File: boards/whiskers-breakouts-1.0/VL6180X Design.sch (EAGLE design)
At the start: 17 parts, among them Q1 BSS138, Q2 BSS138, U1 VL6180X, U3 MIC5225_2.8V, U4 VL6180X, U5 VL6180X

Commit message: Whiskers update
Updated the Whiskers board: routing and asthetics
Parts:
- removed C4, C6: 10uF, SparkFun-Capacitors:1.0NF/1000PF-0603-50V-10%
- removed C5: 0.1uF, SparkFun-Capacitors:1.0NF/1000PF-0603-50V-10%
- removed JP2: (no value), adafruit:PINHD-1X8BIG
- removed Q1, Q2: BSS138, microbuilder:MOSFET-NWIDE
- removed U$10: PINHD-1X10, adafruit:PINHD-1X10
- removed U3: MIC5225_2.8V, microbuilder:VREG_SOT23-5
- removed U4, U5: VL6180X, microbuilder:VL6180X
- added C3: 10uF, SparkFun-Capacitors:1.0NF/1000PF-0603-50V-10%
- added J1: FEMALE 2x3, SparkFun-Connectors:CONN_03X2FEMALE
- added Q3, Q4: BSS138, microbuilder:MOSFET-NWIDE
- added U2: MIC5225_2.8V, microbuilder:VREG_SOT23-5
- C1: value 0.1uF -> 10uF
- R1, R2, R3, R4: device adafruit:FLIPFLOP-RES -> SparkFun-Resistors:0.05OHM-0603-1/5W-1%
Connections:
- removed net INT_1: U1.GPIO1
- removed net INT_2: U5.GPIO1
- removed net INT_3: U4.GPIO1
- removed net N$10: U$10.9
- removed net N$5: U$10.6
- removed net N$6: JP2.6
- removed net N$7: JP2.7
- removed net N$8: U$10.7
- removed net N$9: U$10.8
- removed net OUT: C4.2, U3.OUT
- removed net RESET_1: U1.GPIO0
- removed net RESET_2: U5.GPIO0
- removed net RESET_3: U4.GPIO0
- new net VCC: C1.2, R1.2, R4.2, U2.OUT
- net +3.3V: now also C3.2, J1.1, Q3.G, Q4.G, U2.EN, U2.IN; no longer C1.1, C5.1, C6.2, JP2.1, Q1.G, Q2.G, R1.2, R4.2, U$10.1, U3.EN, U3.IN, U4.AVDD, U4.AVDD_VCS, U5.AVDD, U5.AVDD_VCS
- net GND: now also C1.1, C3.1, J1.6, U2.GND; no longer C1.2, C4.1, C5.2, C6.1, JP2.8, U$10.10, U3.GND, U4.AVSS, U4.AVSS_VCS, U5.AVSS, U5.AVSS_VCS
- net INT: now also J1.3, U1.GPIO1; no longer JP2.3, U$10.3
- net RST: now also J1.2, U1.GPIO0; no longer JP2.2, U$10.2
- net SCL_2.7V: now also Q3.S; no longer Q1.S, Q2.S, R1.1, U4.SCL, U5.SCL
- net SCL_3.3V: now also J1.4, Q3.D; no longer JP2.4, Q1.D, Q2.D, R2.1, U$10.4
- net SDA_2.7V: now also Q4.S, R2.1; no longer U4.SDA, U5.SDA
- net SDA_3.3V: now also J1.5, Q4.D, R1.1; no longer JP2.5, U$10.5
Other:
- note added: "Bi-directional LevelSshifter"
- note added: "Connector"
- note added: "Sensor"
- note added: "Voltage Regulator"

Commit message: adding one more sensor
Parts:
- added C4, C5: 0.1uF, SparkFun-Capacitors:1.0NF/1000PF-0603-50V-10%
- added R5, R6, R7: 47k, SparkFun-Resistors:0.05OHM-0603-1/5W-1%
- added U3, U4: VL6180X, microbuilder:VL6180X
- J1: value FEMALE 2x3 -> 7-PIN_2MM-V; device SparkFun-Connectors:CONN_03X2FEMALE -> RoboJackets-Connectors:7-PIN_2MM-V
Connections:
- removed net RST: J1.2, U1.GPIO0
- new net N$1: R5.2, U1.GPIO0
- new net N$2: R6.2, U3.GPIO0
- new net N$3: R7.2, U4.GPIO0
- new net RST_1: J1.2, R5.1
- new net RST_2: J1.3, R6.1
- new net RST_3: R7.1
- net +3.3V: now also C4.1, C5.1, U3.AVDD, U3.AVDD_VCS, U4.AVDD, U4.AVDD_VCS
- net GND: now also C4.2, C5.2, J1.7, U3.AVSS, U3.AVSS_VCS, U4.AVSS, U4.AVSS_VCS; no longer J1.6
- net INT: now also J1.4, U3.GPIO1, U4.GPIO1; no longer J1.3
- net SCL_2.7V: now also U3.SCL, U4.SCL
- net SCL_3.3V: now also J1.5; no longer J1.4
- net SDA_2.7V: now also U3.SDA, U4.SDA
- net SDA_3.3V: now also J1.6; no longer J1.5
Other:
- moved on the sheet: C2, U1

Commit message: latest
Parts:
- removed J1: 7-PIN_2MM-V, RoboJackets-Connectors:7-PIN_2MM-V
- added J2: 6-PIN_2MM-V, RoboJackets-Connectors:6-PIN_2MM-V
- C1, C3: value 10uF -> 1uF
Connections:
- net SCL_2.7V renamed SCL_2.8V
- net SDA_2.7V renamed SDA_2.8V
- removed net INT: J1.4, U1.GPIO1, U3.GPIO1, U4.GPIO1
- removed net N$1: R5.2, U1.GPIO0
- removed net N$2: R6.2, U3.GPIO0
- removed net N$3: R7.2, U4.GPIO0
- net +3.3V: now also J2.1; no longer C2.1, C4.1, C5.1, J1.1, U1.AVDD, U1.AVDD_VCS, U3.AVDD, U3.AVDD_VCS, U4.AVDD, U4.AVDD_VCS
- net GND: now also J2.6; no longer J1.7
- net RST_1: now also J2.2, U1.GPIO0; no longer J1.2
- net RST_2: now also J2.3, R6.2, U3.GPIO0; no longer J1.3, R6.1
- net RST_3: now also R7.2, U4.GPIO0; no longer R7.1
- net SCL_3.3V: now also J2.4; no longer J1.5
- net SDA_3.3V: now also J2.5; no longer J1.6
- net VCC: now also C2.1, C4.1, C5.1, R5.2, R6.1, R7.1, U1.AVDD, U1.AVDD_VCS, U3.AVDD, U3.AVDD_VCS, U4.AVDD, U4.AVDD_VCS
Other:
- moved on the sheet: C1, C2, C3, C4, C5, Q3, Q4, R1, R2, R3, R4, R5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

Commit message: Board Design Draft
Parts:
- R1: device SparkFun-Resistors:0.05OHM-0603-1/5W-1% -> RoboJackets-Resistors:R0603W
- R2, R3, R4: value 10k -> 4.7k; device SparkFun-Resistors:0.05OHM-0603-1/5W-1% -> RoboJackets-Resistors:R0603W
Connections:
- net +3.3V: now also R2.PIN2, R3.PIN2; no longer R2.2, R3.2
- net SCL_2.8V: now also R3.PIN1; no longer R3.1
- net SCL_3.3V: now also R4.PIN1; no longer R4.1
- net SDA_2.8V: now also R2.PIN1; no longer R2.1
- net SDA_3.3V: now also R1.PIN1; no longer R1.1
- net VCC: now also R1.PIN2, R4.PIN2; no longer R1.2, R4.2
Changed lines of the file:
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@@
 <?xml version="1.0" encoding="utf-8"?>
 <!DOCTYPE eagle SYSTEM "eagle.dtd">
-<eagle version="9.5.1">
+<eagle version="9.6.2">
 <drawing>
 <settings>
@@
 <setting verticaltext="up"/>
 </settings>
-<grid distance="0.1" unitdist="inch" unit="inch" style="lines" multiple="1" display="yes" altdistance="0.01" altunitdist="inch" altunit="inch"/>
+<grid distance="0.1" unitdist="inch" unit="inch" style="lines" multiple="1" display="no" altdistance="0.01" altunitdist="inch" altunit="inch"/>
 <layers>
 <layer number="1" name="Top" color="4" fill="1" visible="no" active="no"/>
@@
 <part name="U$1" library="microbuilder" deviceset="GND" device=""/>
 <part name="U$3" library="microbuilder" deviceset="GND" device=""/>
-<part name="R1" library="SparkFun-Resistors" library_urn="urn:adsk.eagle:library:532" deviceset="0.05OHM" device="-0603-1/5W-1%" package3d_urn="urn:adsk.eagle:package:39650/1" value="10k"/>
-<part name="R2" library="SparkFun-Resistors" library_urn="urn:adsk.eagle:library:532" deviceset="0.05OHM" device="-0603-1/5W-1%" package3d_urn="urn:adsk.eagle:package:39650/1" value="10k"/>
-<part name="R3" library="SparkFun-Resistors" library_urn="urn:adsk.eagle:library:532" deviceset="0.05OHM" device="-0603-1/5W-1%" package3d_urn="urn:adsk.eagle:package:39650/1" value="10k"/>
-<part name="R4" library="SparkFun-Resistors" library_urn="urn:adsk.eagle:library:532" deviceset="0.05OHM" device="-0603-1/5W-1%" package3d_urn="urn:adsk.eagle:package:39650/1" value="10k"/>
+<part name="R1" library="RoboJackets-Resistors" deviceset="R0603W" device="" value="10k"/>
+<part name="R2" library="RoboJackets-Resistors" deviceset="R0603W" device="" value="4.7k"/>
+<part name="R3" library="RoboJackets-Resistors" deviceset="R0603W" device="" value="4.7k"/>
+<part name="R4" library="RoboJackets-Resistors" deviceset="R0603W" device="" value="4.7k"/>
 <part name="P+1" library="supply1" library_urn="urn:adsk.eagle:library:371" deviceset="VCC" device="" value="+2.8V"/>
 <part name="P+2" library="supply1" library_urn="urn:adsk.eagle:library:371" deviceset="VCC" device="" value="+2.8V"/>
@@
 </instance>
 <instance part="R1" gate="G$1" x="149.86" y="142.24" smashed="yes" rot="R90">
-<attribute name="NAME" x="148.336" y="142.24" size="1.778" layer="95" font="vector" rot="R90" align="bottom-center"/>
-<attribute name="VALUE" x="151.384" y="142.24" size="1.778" layer="96" font="vector" rot="R90" align="top-center"/>
+<attribute name="NAME" x="148.3614" y="138.43" size="1.778" layer="95" rot="R90"/>
+<attribute name="VALUE" x="153.162" y="138.43" size="1.778" layer="96" rot="R90"/>
 </instance>
 <instance part="R2" gate="G$1" x="119.38" y="142.24" smashed="yes" rot="R90">
-<attribute name="NAME" x="117.856" y="142.24" size="1.778" layer="95" font="vector" rot="R90" align="bottom-center"/>
-<attribute name="VALUE" x="120.904" y="142.24" size="1.778" layer="96" font="vector" rot="R90" align="top-center"/>
+<attribute name="NAME" x="117.8814" y="138.43" size="1.778" layer="95" rot="R90"/>
+<attribute name="VALUE" x="122.682" y="138.43" size="1.778" layer="96" rot="R90"/>
 </instance>
 <instance part="R3" gate="G$1" x="119.38" y="185.42" smashed="yes" rot="R90">
-<attribute name="NAME" x="117.856" y="185.42" size="1.778" layer="95" font="vector" rot="R90" align="bottom-center"/>
-<attribute name="VALUE" x="120.904" y="185.42" size="1.778" layer="96" font="vector" rot="R90" align="top-center"/>
+<attribute name="NAME" x="117.8814" y="181.61" size="1.778" layer="95" rot="R90"/>
+<attribute name="VALUE" x="122.682" y="181.61" size="1.778" layer="96" rot="R90"/>
 </instance>
 <instance part="R4" gate="G$1" x="149.86" y="185.42" smashed="yes" rot="R90">
-<attribute name="NAME" x="148.336" y="185.42" size="1.778" layer="95" font="vector" rot="R90" align="bottom-center"/>
-<attribute name="VALUE" x="151.384" y="185.42" size="1.778" layer="96" font="vector" rot="R90" align="top-center"/>
+<attribute name="NAME" x="148.3614" y="181.61" size="1.778" layer="95" rot="R90"/>
+<attribute name="VALUE" x="153.162" y="181.61" size="1.778" layer="96" rot="R90"/>
 </instance>
 <instance part="P+1" gate="VCC" x="238.76" y="121.92" smashed="yes">
@@
 <wire x1="134.62" y1="193.04" x2="119.38" y2="193.04" width="0.1524" layer="91"/>
 <junction x="119.38" y="193.04"/>
-<pinref part="R3" gate="G$1" pin="2"/>
+<pinref part="R3" gate="G$1" pin="PIN2"/>
 </segment>
 <segment>
@@
 <wire x1="134.62" y1="149.86" x2="119.38" y2="149.86" width="0.1524" layer="91"/>
 <junction x="119.38" y="149.86"/>
-<pinref part="R2" gate="G$1" pin="2"/>
+<pinref part="R2" gate="G$1" pin="PIN2"/>
 </segment>
 <segment>
@@
 <wire x1="149.86" y1="180.34" x2="149.86" y2="172.72" width="0.1524" layer="91"/>
 <junction x="149.86" y="172.72"/>
-<pinref part="R4" gate="G$1" pin="1"/>
+<pinref part="R4" gate="G$1" pin="PIN1"/>
 </segment>
 <segment>
@@
 <wire x1="149.86" y1="137.16" x2="149.86" y2="129.54" width="0.1524" layer="91"/>
 <junction x="149.86" y="129.54"/>
-<pinref part="R1" gate="G$1" pin="1"/>
+<pinref part="R1" gate="G$1" pin="PIN1"/>
 </segment>
 <segment>
@@
 <segment>
 <wire x1="149.86" y1="147.32" x2="149.86" y2="154.94" width="0.1524" layer="91"/>
-<pinref part="R1" gate="G$1" pin="2"/>
+<pinref part="R1" gate="G$1" pin="PIN2"/>
 <pinref part="P+2" gate="VCC" pin="VCC"/>
 </segment>
 <segment>
 <wire x1="149.86" y1="190.5" x2="149.86" y2="198.12" width="0.1524" layer="91"/>
-<pinref part="R4" gate="G$1" pin="2"/>
+<pinref part="R4" gate="G$1" pin="PIN2"/>
 <pinref part="P+3" gate="VCC" pin="VCC"/>
 </segment>
@@
 <wire x1="119.38" y1="137.16" x2="119.38" y2="129.54" width="0.1524" layer="91"/>
 <junction x="119.38" y="129.54"/>
-<pinref part="R2" gate="G$1" pin="1"/>
+<pinref part="R2" gate="G$1" pin="PIN1"/>
 </segment>
 <segment>
@@
 <wire x1="119.38" y1="180.34" x2="119.38" y2="172.72" width="0.1524" layer="91"/>
 <junction x="119.38" y="172.72"/>
-<pinref part="R3" gate="G$1" pin="1"/>
-</segment>
-<segment>
+<pinref part="R3" gate="G$1" pin="PIN1"/>
+</segment>
+<segment>

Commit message: Board Draft 2
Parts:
- R1: value 10k -> 4.7k
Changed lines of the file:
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@@
 <part name="U$1" library="microbuilder" deviceset="GND" device=""/>
 <part name="U$3" library="microbuilder" deviceset="GND" device=""/>
-<part name="R1" library="RoboJackets-Resistors" deviceset="R0603W" device="" value="10k"/>
+<part name="R1" library="RoboJackets-Resistors" deviceset="R0603W" device="" value="4.7k"/>
 <part name="R2" library="RoboJackets-Resistors" deviceset="R0603W" device="" value="4.7k"/>
 <part name="R3" library="RoboJackets-Resistors" deviceset="R0603W" device="" value="4.7k"/>

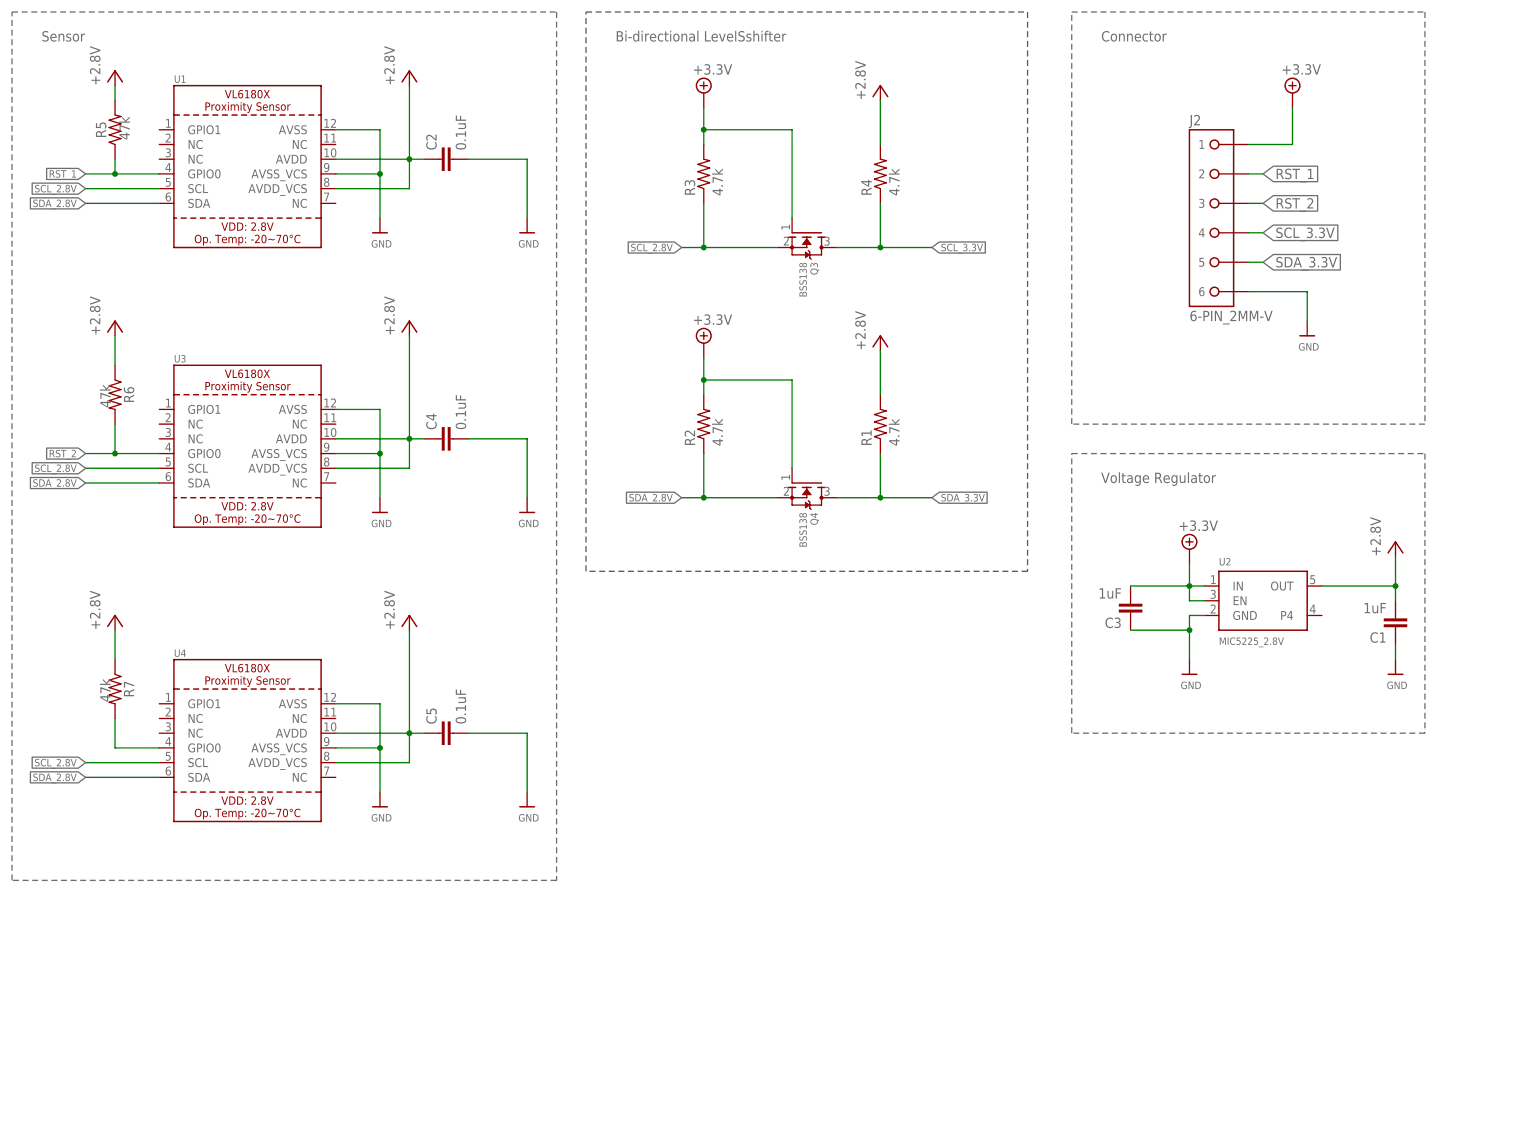
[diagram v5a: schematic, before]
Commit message: Schematic Correction
Added Capacitors to VL6180X to match typical application schematic found on datasheet. Fixed ports on MOLEX to align with control boards i2c port (swapped SDA and SCL, change 3.3V to 5V). Added additional voltage regulator to step down 5V to 3.3V.
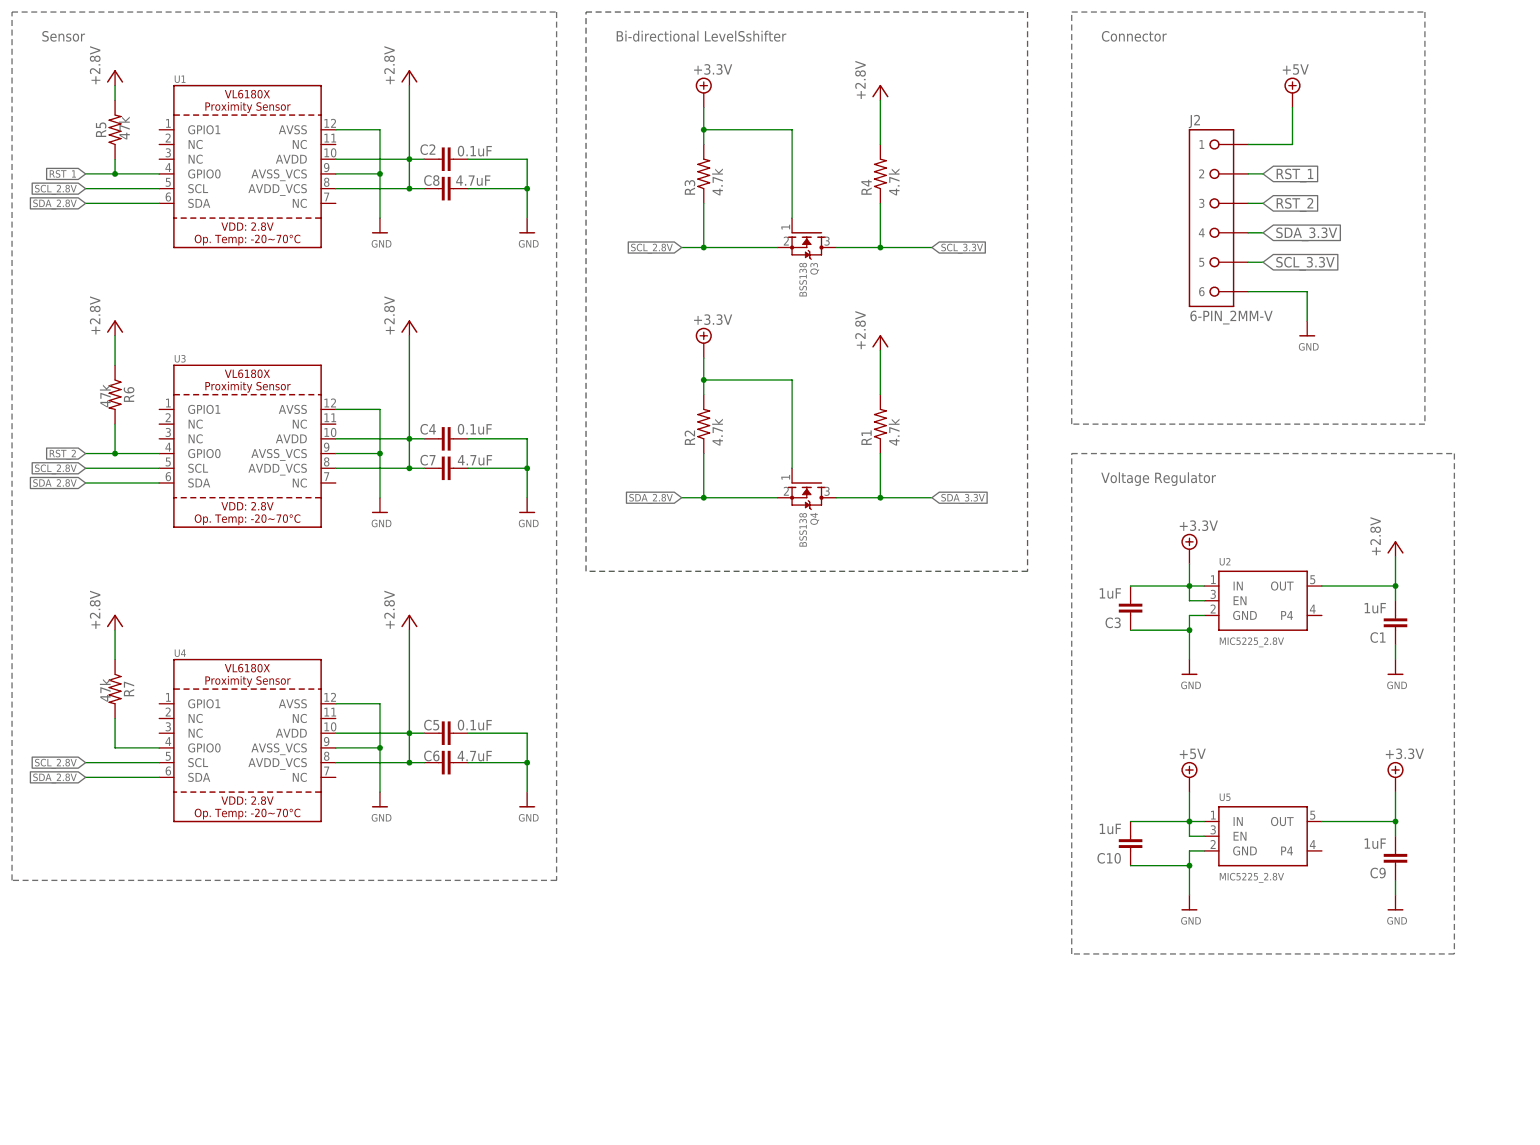
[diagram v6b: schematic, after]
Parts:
- added C10, C9: 1uF, SparkFun-Capacitors:1.0NF/1000PF-0603-50V-10%
- added C6, C7, C8: 4.7uF, SparkFun-Capacitors:1.0NF/1000PF-0603-50V-10%
- added U5: MIC5225_2.8V, microbuilder:VREG_SOT23-5
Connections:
- new net +5V: C10.2, J2.1, U5.EN, U5.IN
- net +3.3V: now also C9.2, U5.OUT; no longer J2.1
- net GND: now also C10.1, C6.2, C7.2, C8.2, C9.1, U5.GND
- net SCL_3.3V: now also J2.5; no longer J2.4
- net SDA_3.3V: now also J2.4; no longer J2.5
- net VCC: now also C6.1, C7.1, C8.1

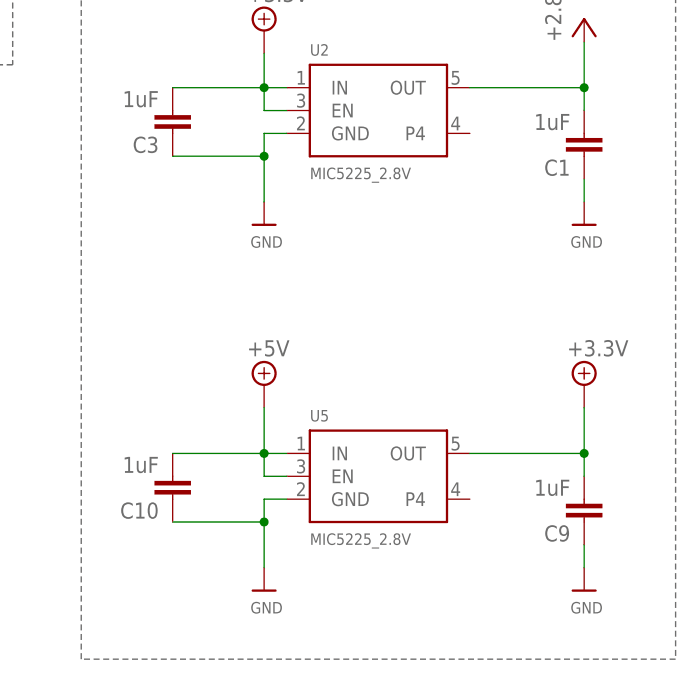
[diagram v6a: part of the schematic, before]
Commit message: Naming Components
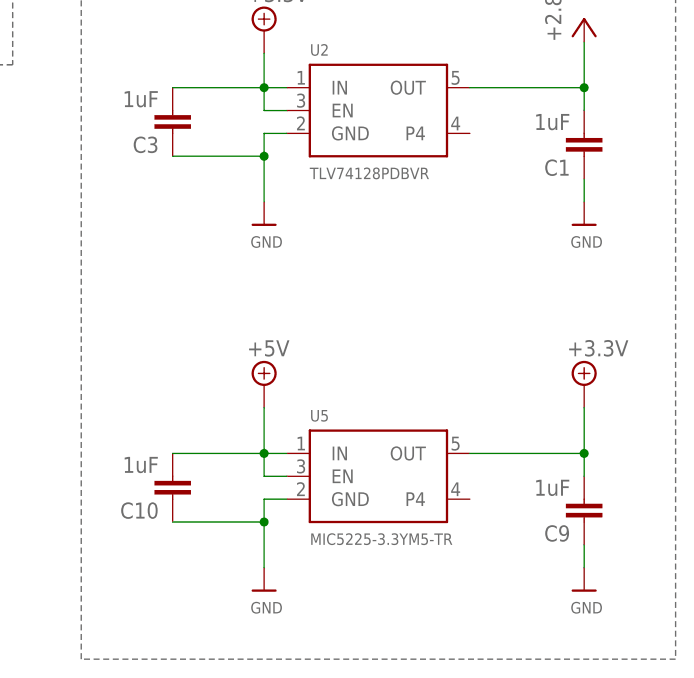
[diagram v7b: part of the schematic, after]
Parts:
- U2: value MIC5225_2.8V -> TLV74128PDBVR
- U5: value MIC5225_2.8V -> MIC5225-3.3YM5-TR
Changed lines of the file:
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@@
 <part name="Q4" library="microbuilder" deviceset="MOSFET-N" device="WIDE" value="BSS138"/>
 <part name="SUPPLY11" library="RoboJackets-Supplies" deviceset="+3.3V" device="" value="+3.3V"/>
-<part name="U2" library="microbuilder" deviceset="VREG_SOT23-5" device="" value="MIC5225_2.8V"/>
+<part name="U2" library="microbuilder" deviceset="VREG_SOT23-5" device="" value="TLV74128PDBVR"/>
 <part name="SUPPLY13" library="RoboJackets-Supplies" deviceset="+3.3V" device="" value="+3.3V"/>
 <part name="C1" library="SparkFun-Capacitors" library_urn="urn:adsk.eagle:library:510" deviceset="1.0NF/1000PF" device="-0603-50V-10%" package3d_urn="urn:adsk.eagle:package:37414/1" value="1uF"/>
@@
 <part name="C7" library="SparkFun-Capacitors" library_urn="urn:adsk.eagle:library:510" deviceset="1.0NF/1000PF" device="-0603-50V-10%" package3d_urn="urn:adsk.eagle:package:37414/1" value="4.7uF"/>
 <part name="C8" library="SparkFun-Capacitors" library_urn="urn:adsk.eagle:library:510" deviceset="1.0NF/1000PF" device="-0603-50V-10%" package3d_urn="urn:adsk.eagle:package:37414/1" value="4.7uF"/>
-<part name="U5" library="microbuilder" deviceset="VREG_SOT23-5" device="" value="MIC5225_2.8V"/>
+<part name="U5" library="microbuilder" deviceset="VREG_SOT23-5" device="" value="MIC5225-3.3YM5-TR"/>
 <part name="SUPPLY3" library="RoboJackets-Supplies" deviceset="+3.3V" device="" value="+3.3V"/>
 <part name="C9" library="SparkFun-Capacitors" library_urn="urn:adsk.eagle:library:510" deviceset="1.0NF/1000PF" device="-0603-50V-10%" package3d_urn="urn:adsk.eagle:package:37414/1" value="1uF"/>
